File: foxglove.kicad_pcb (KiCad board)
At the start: 4 copper layers, 70.7 x 53.3 mm, 140 parts, among them IC1 LFE5U-12F-6BG256C, J1 NEIGHBOR1, J2 NEIGHBOR2, J3 Conn_02x05_Odd_Even, J4 Conn_02x05_Odd_Even, J5 Conn_01x02_Female, J6 Conn_02x03_Odd_Even, J7 BONUS_ROW, U1 LM393, U10 SHIFTER, U11 74HC4051, U12 SHIFTER, U13 74HC4051, U14 SHIFTER, U15 74HC4051, U16 SHIFTER, U17 74HC4051, U18 SHIFTER, U19 74HC4051, U2 ADP225, U20 SHIFTER, U21 74HC4051, U22 SHIFTER, U23 74HC4051, U24 SHIFTER, U25 74LVC1G53, U3 AP2127, U4 74LVC1G3157, U5 AP2127, U6 AP2127, U7 DAC084S085, U9 74HC4051

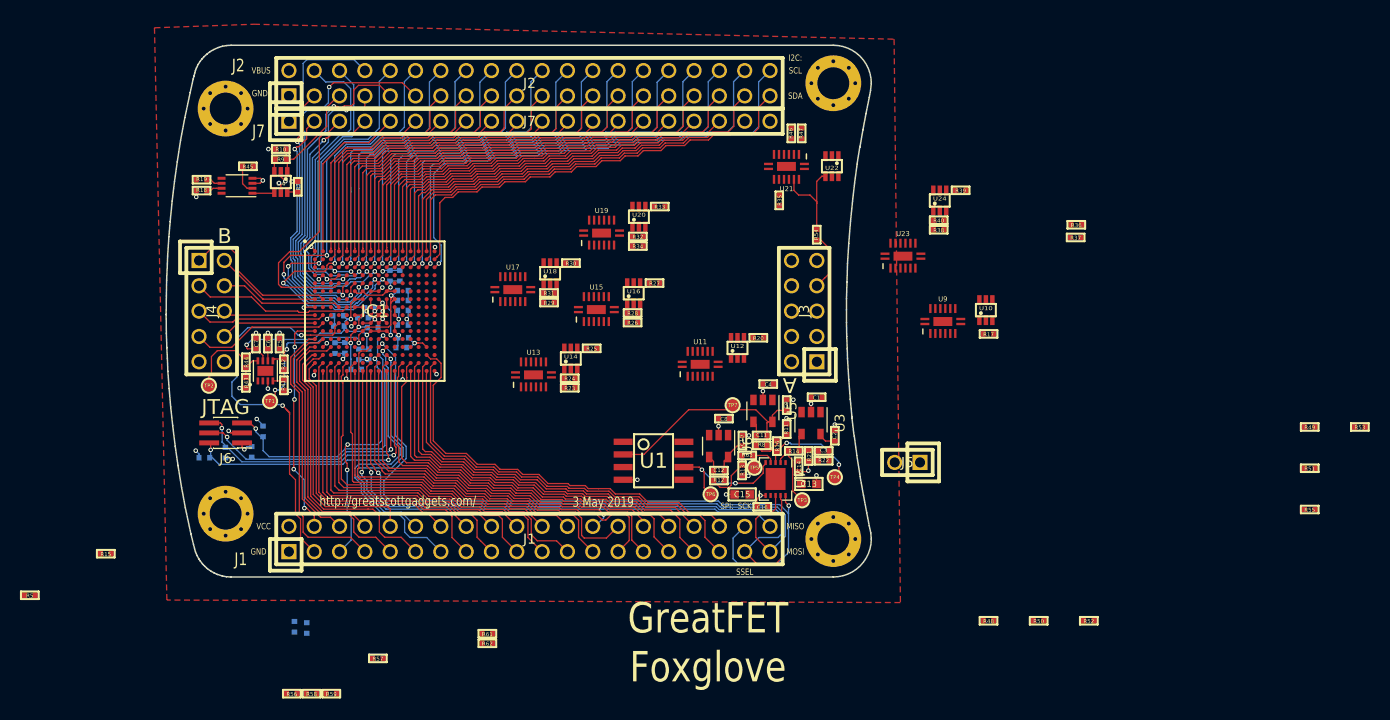
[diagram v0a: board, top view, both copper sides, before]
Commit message: Fixed sym-lib-table and continued routing bank A
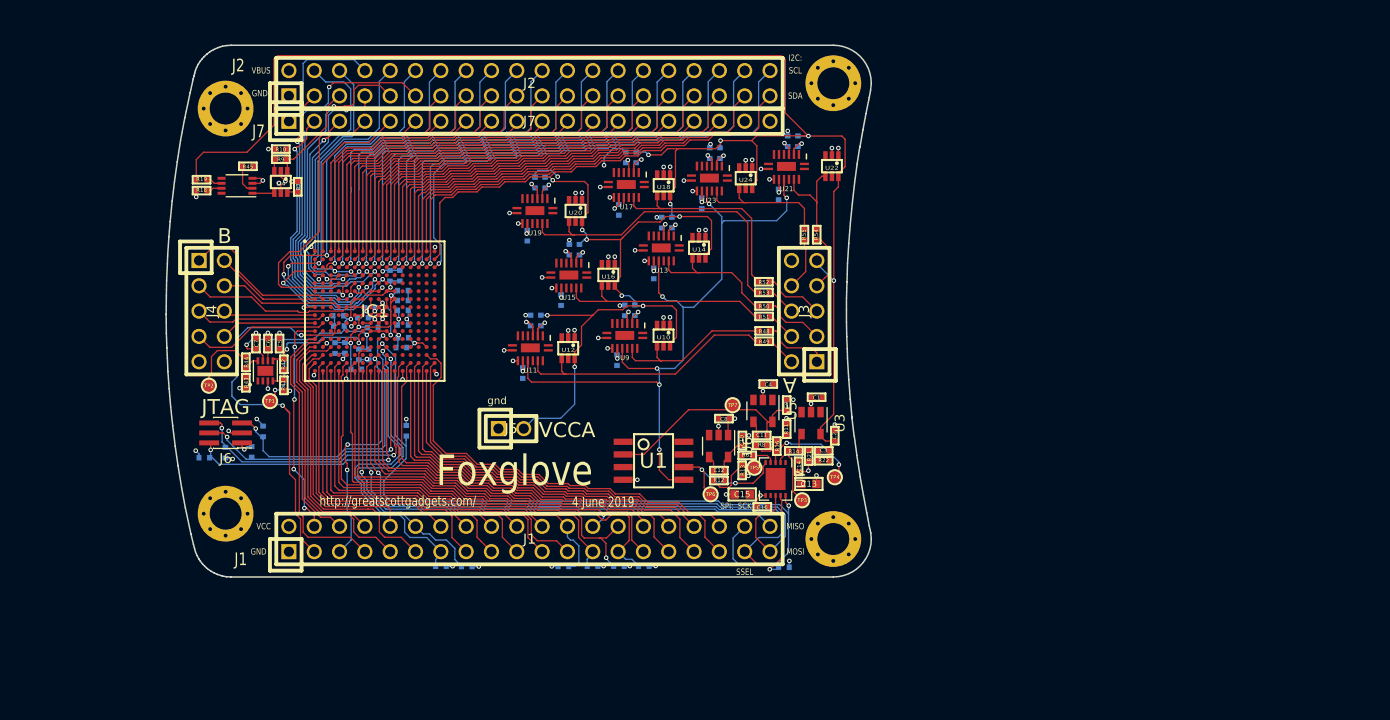
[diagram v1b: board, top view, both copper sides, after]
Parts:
- R15, R17, R20, R23, R24, R25, R26, R27, R28, R29, R30, R31, R32, R33, R34, R35, R36, R37, R38, R39, R40, R46, R47, R5, R56, R57, R58, R59, R61, R62: moved to B.Cu
- moved R15 68.0 mm to (171.6, 120.9), turned to 180 degrees
- moved R5 61.7 mm to (157.5, 120.8), turned to 180 degrees
- moved R53 61.3 mm to (169.6, 93.4)
- moved R55 57.7 mm to (173.6, 87.6), turned to 270 degrees
- moved R51 56.8 mm to (169.6, 95.8)
- moved R49 55.4 mm to (169.6, 98.3)
- moved R62 54.4 mm to (165.2, 79.4), turned to 270 degrees
- moved R61 53.1 mm to (164.1, 79.4), turned to 270 degrees
- moved R52 47.1 mm to (169.6, 92.3)
- moved R36 45.7 mm to (155.7, 79.8), turned to 270 degrees
- moved R37 44.8 mm to (156.8, 79.8), turned to 270 degrees
- moved R39 42.7 mm to (146.6, 82.4), turned to 270 degrees
- moved R50 41.9 mm to (169.6, 94.7)
- moved J5 39.9 mm to (144.2, 107.0), turned to 0 degrees
- moved R40 39.7 mm to (147.6, 82.4), turned to 270 degrees
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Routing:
- net /VCCA: track 4.07 -> 224.9 mm, vias 0 -> 13
- net /COMP2: track 0.00 -> 73.5 mm, vias 0 -> 6
- net Net-(R53-Pad1): track 0.00 -> 32.4 mm
- net GND: track 59.9 -> 87.1 mm, vias 46 -> 80
- net Net-(R49-Pad1): track 0.00 -> 27.0 mm
- net Net-(R51-Pad1): track 0.00 -> 21.9 mm
- net Net-(R52-Pad1): track 0.00 -> 21.7 mm
- net Net-(R48-Pad1): track 0.00 -> 16.8 mm
- net Net-(R55-Pad1): track 0.00 -> 14.0 mm
- net Net-(R50-Pad1): track 0.00 -> 14.0 mm
- net VCC: track 27.1 -> 39.0 mm, vias 10 -> 24
- net /CFG_1: track 25.1 -> 32.0 mm
- net /A1: track 0.00 -> 6.92 mm
- net /A3: track 0.00 -> 6.38 mm
- net /A5: track 0.00 -> 6.21 mm
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- removed copper zone on F.Cu, net +5V
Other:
- board text added: "4 June 2019"
- board text added: "Foxglove"
- board text added: "VCCA"
- board text added: "gnd"
- board text removed: "3 May 2019"
- board text removed: "GreatFET Foxglove"

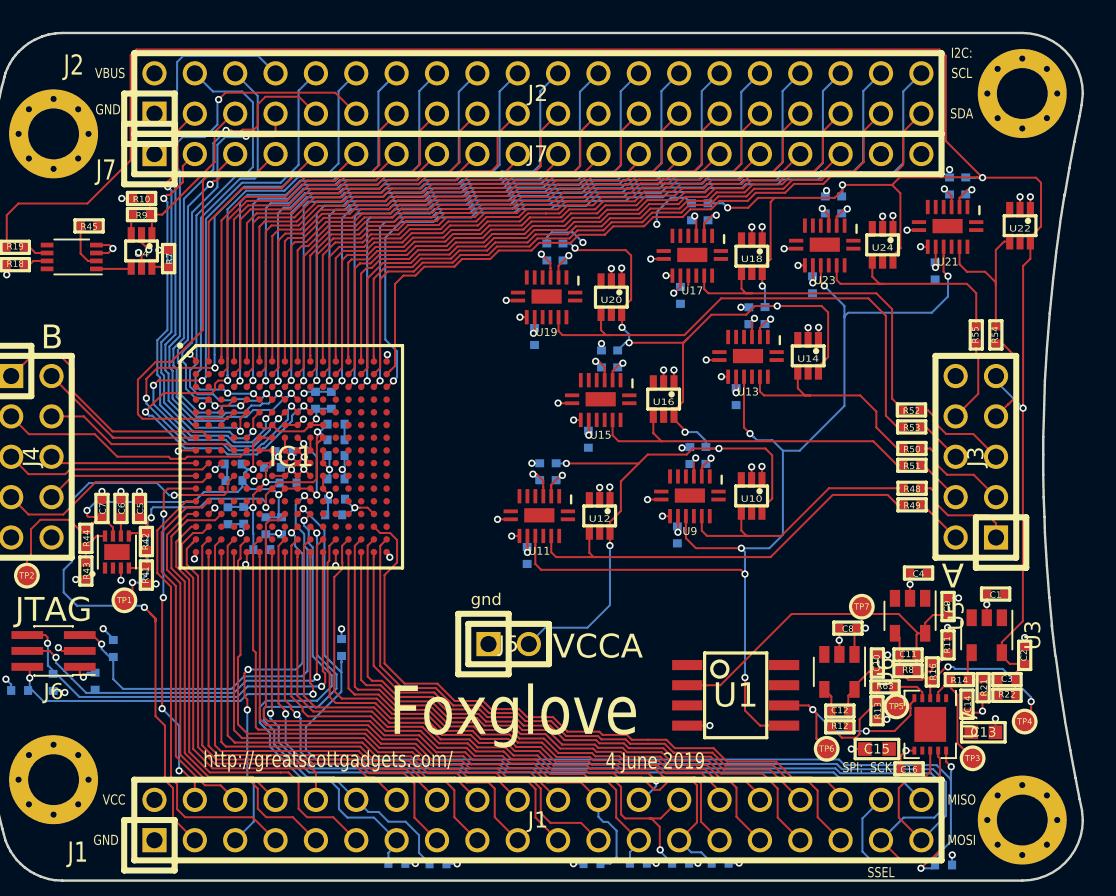
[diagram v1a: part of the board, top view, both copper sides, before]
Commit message: Changed headers for bank A and B, combined ADC voltage divider / pull-ups
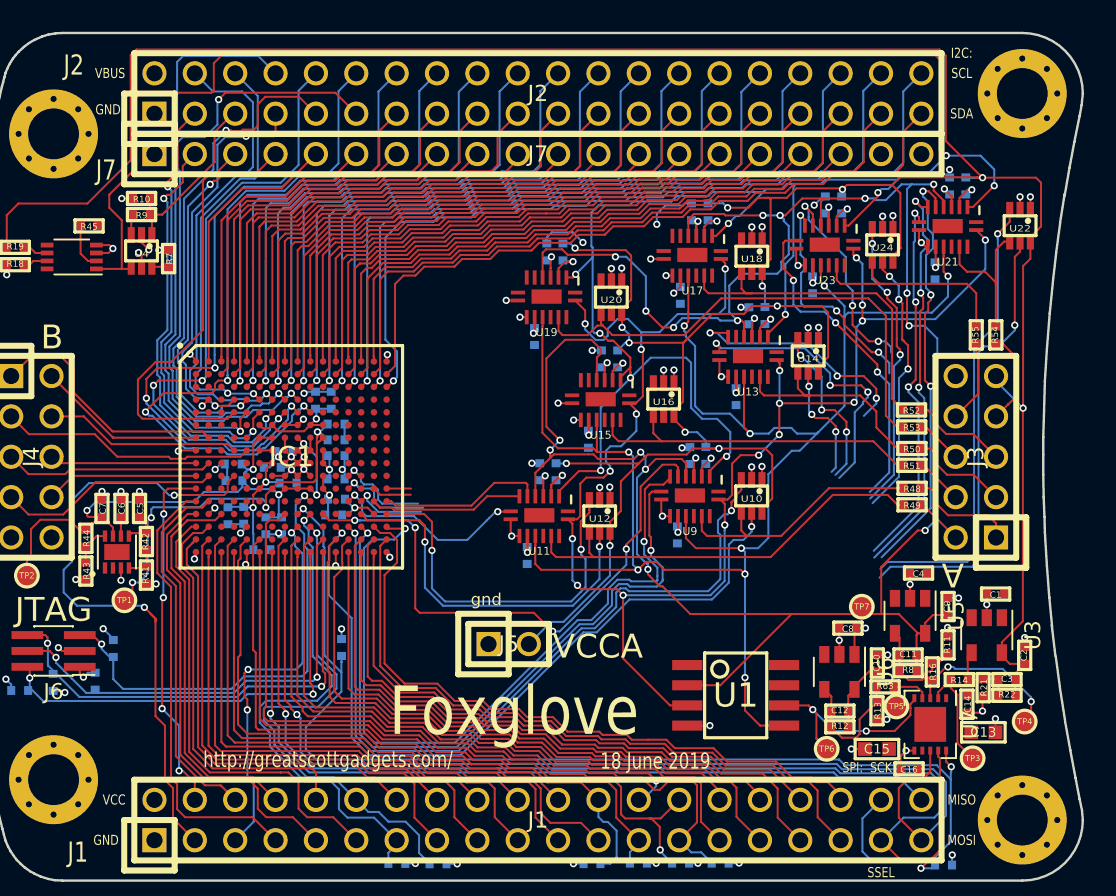
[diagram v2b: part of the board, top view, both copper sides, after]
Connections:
- IC1 pad K13: (no net) -> /S0_3
- IC1 pad L13: (no net) -> /S1_3
- IC1 pad L15: (no net) -> /DIR_3
- IC1 pad L16: (no net) -> /A3_shift
- IC1 pad M13: (no net) -> /S2_2
- IC1 pad M14: (no net) -> /S2_3
- IC1 pad M15: (no net) -> /S1_2
- IC1 pad M16: (no net) -> /S0_2
- IC1 pad N11: (no net) -> /S0_1
- IC1 pad N14: (no net) -> /DIR_2
- IC1 pad N16: (no net) -> /A2_shift
- IC1 pad P12: (no net) -> /DIR_1
- IC1 pad P13: (no net) -> /A1_shift
- IC1 pad P14: (no net) -> /S2_1
- IC1 pad P16: (no net) -> /S1_1
- U10 pad 3: (no net) -> /A1_shift
- U10 pad 5: (no net) -> /DIR_1
- U11 pad 10: (no net) -> /S1_2
- U11 pad 11: (no net) -> /S0_2
- U11 pad 9: (no net) -> /S2_2
- U12 pad 3: (no net) -> /A2_shift
- U12 pad 5: (no net) -> /DIR_2
- U13 pad 10: (no net) -> /S1_3
- U13 pad 11: (no net) -> /S0_3
- U13 pad 9: (no net) -> /S2_3
- U14 pad 3: (no net) -> /A3_shift
- U14 pad 5: (no net) -> /DIR_3
- U9 pad 10: (no net) -> /S1_1
- U9 pad 11: (no net) -> /S0_1
- U9 pad 9: (no net) -> /S2_1
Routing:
- net (no net): track 0.00 -> 217.4 mm, vias 0 -> 26
- net /ADC_A: track 2.25 -> 162.7 mm, vias 0 -> 10
- net /DAC: track 22.7 -> 148.1 mm, vias 0 -> 16
- net /COMP1: track 0.00 -> 99.1 mm, vias 0 -> 18
- net /A1_shift: track 0.00 -> 48.9 mm, vias 0 -> 2
- net /DIR_1: track 0.00 -> 48.5 mm, vias 0 -> 2
- net /S1_1: track 0.00 -> 47.6 mm, vias 0 -> 2
- net /S2_1: track 0.00 -> 44.4 mm, vias 0 -> 2
- net /COMP2: track 73.5 -> 110.9 mm, vias 6 -> 9
- net /S0_1: track 0.00 -> 35.7 mm, vias 0 -> 4
- net /A2_shift: track 0.00 -> 23.5 mm, vias 0 -> 2
- net /DIR_2: track 0.00 -> 23.3 mm, vias 0 -> 2
- net /S2_3: track 0.00 -> 22.6 mm, vias 0 -> 4
- net /S1_3: track 0.00 -> 21.3 mm, vias 0 -> 4
- net /S2_2: track 0.00 -> 12.6 mm, vias 0 -> 2
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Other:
- board text added: "18 June 2019"
- board text removed: "4 June 2019"

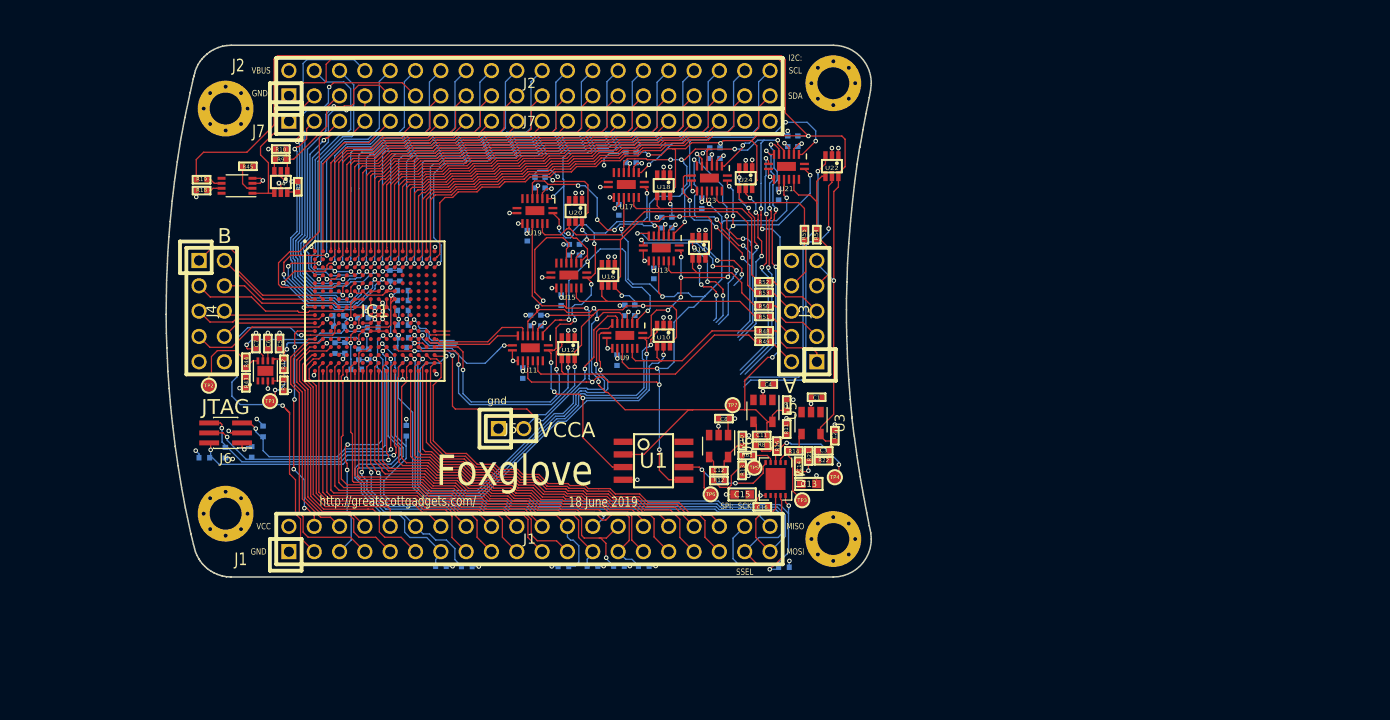
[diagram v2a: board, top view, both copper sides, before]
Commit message: Completed routing of new connectors.
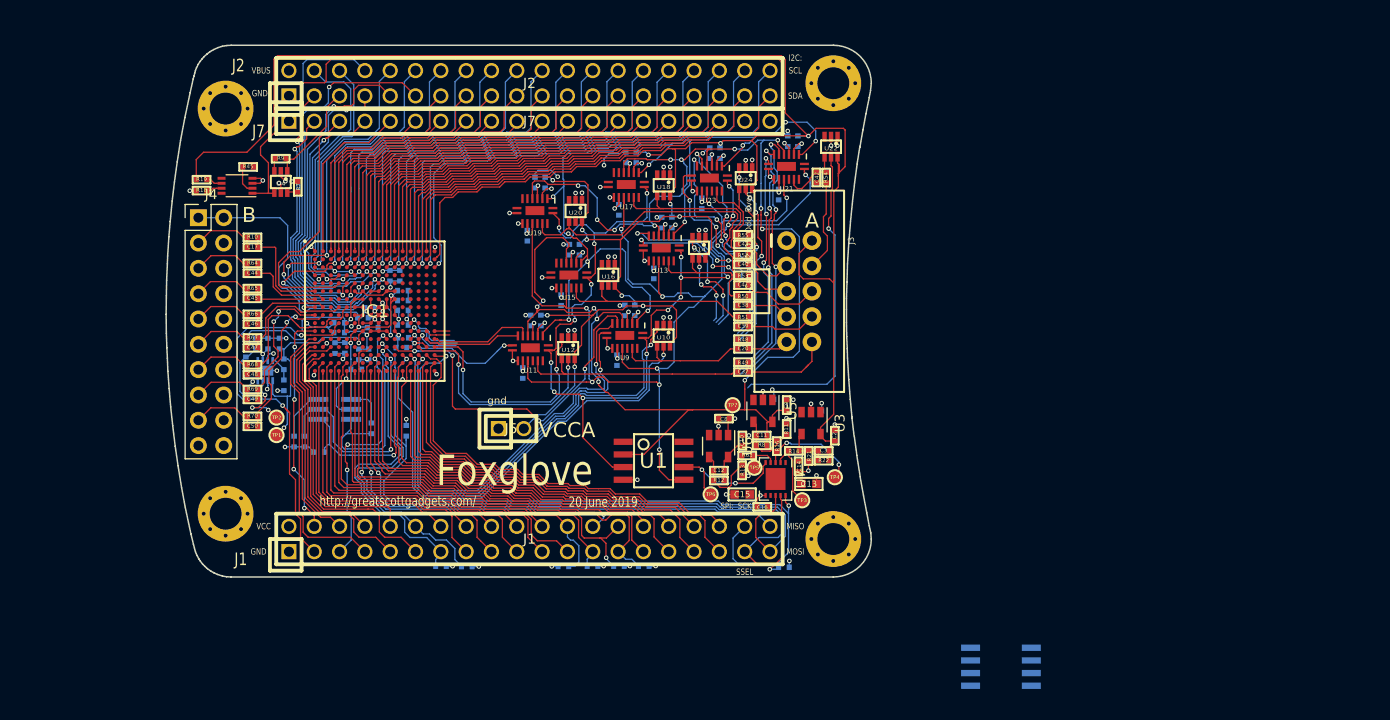
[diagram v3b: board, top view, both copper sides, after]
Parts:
- added C17: 0.1uF, gsg-modules:0402, F.Cu at (118.3, 88.8)
- added C20: 0.1uF, gsg-modules:0402, F.Cu at (167.5, 99.0)
- added C37: 0.1uF, gsg-modules:0402, F.Cu at (167.5, 101.4)
- added C38: 0.1uF, gsg-modules:0402, F.Cu at (167.5, 94.7)
- added C39: 0.1uF, gsg-modules:0402, F.Cu at (167.5, 96.8)
- added C40: 0.1uF, gsg-modules:0402, F.Cu at (167.5, 90.6)
- added C41: 0.1uF, gsg-modules:0402, F.Cu at (167.5, 92.6)
- added C42: 0.1uF, gsg-modules:0402, F.Cu at (174.8, 81.8)
- added C43: 0.1uF, gsg-modules:0402, F.Cu at (167.5, 88.6)
- added C44: 0.1uF, gsg-modules:0402, F.Cu at (118.3, 91.5)
- added C45: 0.1uF, gsg-modules:0402, F.Cu at (118.3, 94.0)
- added C46: 0.1uF, gsg-modules:0402, F.Cu at (118.3, 96.6)
- added C47: 0.1uF, gsg-modules:0402, F.Cu at (118.3, 98.9)
- added C48: 0.1uF, gsg-modules:0402, F.Cu at (118.3, 101.6)
- added C49: 0.1uF, gsg-modules:0402, F.Cu at (118.3, 104.1)
- added C50: 0.1uF, gsg-modules:0402, F.Cu at (118.3, 106.8)
- added R64: 100, gsg-modules:0402, F.Cu at (118.3, 90.5)
- added R65: 100, gsg-modules:0402, F.Cu at (118.3, 93.0)
- added R66: 100, gsg-modules:0402, F.Cu at (118.3, 95.6)
- added R67: 100, gsg-modules:0402, F.Cu at (118.3, 97.9)
- added R68: 100, gsg-modules:0402, F.Cu at (118.3, 100.6)
- added R69: 100, gsg-modules:0402, F.Cu at (118.3, 103.1)
- added R70: 100, gsg-modules:0402, F.Cu at (118.3, 105.8)
- added U8: AT25xxx, gsg-modules:SOIC8-154, B.Cu at (193.3, 130.9)
- C1, C4, C5, C6, C7, J6, R41, R42, R43, R44, U2: moved to B.Cu
- J3: footprint gsg-modules:HEADER-2x5 -> gsg-modules:2X5-SHROUDED
- J4: value Conn_02x05_Odd_Even -> Conn_02x10_Odd_Even; footprint gsg-modules:HEADER-2x5 -> Connector_PinHeader_2.54mm:PinHeader_2x10_P2.54mm_Vertical
- R10: value 10k -> 100
- R48, R49, R50, R51, R52, R53, R54, R55: value 0 -> 100
- moved J6 11.2 mm to (126.5, 105.1)
- moved R60 10.9 mm to (130.2, 107.0)
- moved J4 9.47 mm to (112.8, 85.9), turned to 0 degrees
- moved R1 9.41 mm to (125.0, 109.4), turned to 0 degrees
- moved R10 9.30 mm to (118.3, 87.8), turned to 180 degrees
- moved R2 9.15 mm to (122.4, 108.3), turned to 90 degrees
- moved TP2 7.50 mm to (120.7, 105.9)
- moved R55 6.16 mm to (167.5, 87.6), turned to 0 degrees
- moved R54 5.81 mm to (175.8, 81.9)
- moved R4 5.37 mm to (123.5, 108.3), turned to 90 degrees
- moved TP1 3.46 mm to (120.7, 107.7)
- moved R52 3.41 mm to (167.5, 89.6)
- moved R49 2.98 mm to (167.5, 100.4)
- moved R53 2.71 mm to (167.5, 91.7)
- moved R50 2.34 mm to (167.5, 93.7)
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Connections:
- net /ADC_sel renamed /div_sel
- IC1 pad B1: (no net) -> Net-(IC1-PadB1)
- IC1 pad B2: (no net) -> Net-(IC1-PadB2)
- IC1 pad C1: (no net) -> Net-(IC1-PadC1)
- IC1 pad C2: (no net) -> Net-(IC1-PadC2)
- IC1 pad C3: (no net) -> Net-(IC1-PadC3)
- IC1 pad D1: (no net) -> Net-(IC1-PadD1)
- IC1 pad D10: (no net) -> Net-(IC1-PadD10)
- IC1 pad D11: (no net) -> Net-(IC1-PadD11)
- IC1 pad D12: (no net) -> Net-(IC1-PadD12)
- IC1 pad D13: (no net) -> Net-(IC1-PadD13)
- IC1 pad D14: (no net) -> Net-(IC1-PadD14)
- IC1 pad D16: (no net) -> Net-(IC1-PadD16)
- IC1 pad D3: (no net) -> Net-(IC1-PadD3)
- IC1 pad E1: (no net) -> Net-(IC1-PadE1)
- IC1 pad E11: (no net) -> Net-(IC1-PadE11)
- IC1 pad E12: (no net) -> Net-(IC1-PadE12)
- IC1 pad E13: (no net) -> Net-(IC1-PadE13)
- IC1 pad E14: (no net) -> Net-(IC1-PadE14)
- IC1 pad E15: (no net) -> Net-(IC1-PadE15)
- IC1 pad E16: (no net) -> Net-(IC1-PadE16)
- IC1 pad E2: (no net) -> Net-(IC1-PadE2)
- IC1 pad E3: (no net) -> Net-(IC1-PadE3)
- IC1 pad F1: (no net) -> /B1_P
- IC1 pad F12: (no net) -> Net-(IC1-PadF12)
- IC1 pad F13: (no net) -> Net-(IC1-PadF13)
- IC1 pad F14: (no net) -> Net-(IC1-PadF14)
- IC1 pad F15: (no net) -> Net-(IC1-PadF15)
- IC1 pad F16: (no net) -> Net-(IC1-PadF16)
- IC1 pad F2: (no net) -> Net-(IC1-PadF2)
- IC1 pad F3: (no net) -> Net-(IC1-PadF3)
- IC1 pad F4: (no net) -> Net-(IC1-PadF4)
- IC1 pad F5: (no net) -> Net-(IC1-PadF5)
- IC1 pad G1: /B2 -> /B2_P
- IC1 pad G12: (no net) -> Net-(IC1-PadG12)
- IC1 pad G13: (no net) -> Net-(IC1-PadG13)
- IC1 pad G14: (no net) -> Net-(IC1-PadG14)
- IC1 pad G15: (no net) -> Net-(IC1-PadG15)
- IC1 pad G16: (no net) -> Net-(IC1-PadG16)
- IC1 pad G2: /B1 -> /B1_N
- IC1 pad G3: (no net) -> Net-(IC1-PadG3)
- IC1 pad G4: (no net) -> Net-(IC1-PadG4)
- IC1 pad G5: (no net) -> Net-(IC1-PadG5)
- IC1 pad H12: (no net) -> Net-(IC1-PadH12)
- IC1 pad H13: (no net) -> Net-(IC1-PadH13)
- IC1 pad H14: (no net) -> Net-(IC1-PadH14)
- IC1 pad H15: (no net) -> Net-(IC1-PadH15)
- IC1 pad H2: (no net) -> /B2_N
- IC1 pad H3: (no net) -> Net-(IC1-PadH3)
- IC1 pad H4: /B4 -> /B3_P
- IC1 pad H5: /B3 -> /B3_N
- IC1 pad J1: /B6 -> /B4_P
- IC1 pad J12: (no net) -> Net-(IC1-PadJ12)
- IC1 pad J13: (no net) -> Net-(IC1-PadJ13)
- IC1 pad J14: (no net) -> Net-(IC1-PadJ14)
- IC1 pad J15: (no net) -> Net-(IC1-PadJ15)
- IC1 pad J16: (no net) -> Net-(IC1-PadJ16)
- IC1 pad J2: /B5 -> /B4_N
- IC1 pad J3: (no net) -> Net-(IC1-PadJ3)
- IC1 pad J4: (no net) -> Net-(IC1-PadJ4)
- IC1 pad J5: (no net) -> Net-(IC1-PadJ5)
- IC1 pad K1: /B8 -> Net-(IC1-PadK1)
- IC1 pad K12: (no net) -> Net-(IC1-PadK12)
- IC1 pad K14: (no net) -> Net-(IC1-PadK14)
- IC1 pad K15: (no net) -> Net-(IC1-PadK15)
- IC1 pad K16: (no net) -> Net-(IC1-PadK16)
- IC1 pad K2: /B7 -> Net-(IC1-PadK2)
- IC1 pad K3: (no net) -> Net-(IC1-PadK3)
- IC1 pad K5: (no net) -> Net-(IC1-PadK5)
- IC1 pad L12: (no net) -> Net-(IC1-PadL12)
- IC1 pad L14: (no net) -> Net-(IC1-PadL14)
- IC1 pad L2: (no net) -> Net-(IC1-PadL2)
- IC1 pad L3: (no net) -> Net-(IC1-PadL3)
- IC1 pad L4: (no net) -> Net-(IC1-PadL4)
- IC1 pad L5: (no net) -> Net-(IC1-PadL5)
- IC1 pad M11: (no net) -> Net-(IC1-PadM11)
- IC1 pad M12: (no net) -> Net-(IC1-PadM12)
- IC1 pad M3: (no net) -> Net-(IC1-PadM3)
- IC1 pad M4: (no net) -> Net-(IC1-PadM4)
- IC1 pad M5: (no net) -> Net-(IC1-PadM5)
- IC1 pad M6: (no net) -> Net-(IC1-PadM6)
- IC1 pad M7: (no net) -> Net-(IC1-PadM7)
- IC1 pad M8: (no net) -> Net-(IC1-PadM8)
- IC1 pad M9: (no net) -> Net-(IC1-PadM9)
- IC1 pad N12: (no net) -> Net-(IC1-PadN12)
- IC1 pad N13: (no net) -> Net-(IC1-PadN13)
- IC1 pad N4: (no net) -> Net-(IC1-PadN4)
- IC1 pad N5: (no net) -> Net-(IC1-PadN5)
- IC1 pad N6: (no net) -> Net-(IC1-PadN6)
- IC1 pad N7: (no net) -> Net-(IC1-PadN7)
- IC1 pad P11: (no net) -> Net-(IC1-PadP11)
- IC1 pad P3: (no net) -> Net-(IC1-PadP3)
- IC1 pad P4: (no net) -> Net-(IC1-PadP4)
- IC1 pad P5: (no net) -> Net-(IC1-PadP5)
- IC1 pad P6: (no net) -> Net-(IC1-PadP6)
- IC1 pad P7: (no net) -> Net-(IC1-PadP7)
- IC1 pad P8: (no net) -> Net-(IC1-PadP8)
- IC1 pad R7: (no net) -> Net-(IC1-PadR7)
- J3 pad 1: /A1 -> GND
- J3 pad 10: GND -> /A2
- J3 pad 2: /A2 -> /VCCA
- J3 pad 3: /A3 -> /A8
- J3 pad 4: /A4 -> /A7
- J3 pad 7: /A7 -> /A3
- J3 pad 8: /A8 -> /A4
- J3 pad 9: /VCCA -> /A1
- J4 pad 1: /B1 -> /VCCB
- J4 pad 2: /B2 -> /VCCB
- J4 pad 3: /B3 -> /Sheet5D737161/target
- J4 pad 4: /B4 -> GND
- J4 pad 5: /B5 -> /sheet5D96E709/target
- J4 pad 6: /B6 -> GND
- J4 pad 7: /B7 -> /sheet5D9A1BD9/target
- J4 pad 8: /B8 -> GND
- J4 pad 9: /VCCB -> /sheet5D9A1BDA/target
- R10 pad 1: GND -> /B1_P
- R10 pad 2: /ADC -> /Sheet5D737161/target
- R45 pad 1: /EN_pull -> +5V
- R45 pad 2: +5V -> /pull_en
- R9 pad 1: Net-(R9-Pad1) -> /ADC
- R9 pad 2: /ADC -> Net-(R9-Pad2)
- U1 pad 1: (no net) -> /COUT1
- U1 pad 7: (no net) -> /COUT2
- U11 pad 2: (no net) -> Net-(U11-Pad2)
- U11 pad 4: (no net) -> Net-(U11-Pad4)
- U13 pad 2: (no net) -> Net-(U13-Pad2)
- U13 pad 4: (no net) -> Net-(U13-Pad4)
- U15 pad 10: (no net) -> /S1_4
- U15 pad 11: (no net) -> /S0_4
- U15 pad 2: (no net) -> Net-(U15-Pad2)
- U15 pad 4: (no net) -> Net-(U15-Pad4)
- U15 pad 9: (no net) -> /S2_4
- U16 pad 3: (no net) -> /A4_shift
- U16 pad 5: (no net) -> /DIR_4
- U17 pad 10: (no net) -> /S1_5
- U17 pad 11: (no net) -> /S0_5
- U17 pad 2: (no net) -> Net-(U17-Pad2)
- U17 pad 4: (no net) -> Net-(U17-Pad4)
- U17 pad 9: (no net) -> /S2_5
- U18 pad 3: (no net) -> /A5_shift
- U18 pad 5: (no net) -> /DIR_5
- U19 pad 10: (no net) -> /S1_6
- U19 pad 11: (no net) -> /S0_6
- U19 pad 2: (no net) -> Net-(U19-Pad2)
- U19 pad 4: (no net) -> Net-(U19-Pad4)
- U19 pad 9: (no net) -> /S2_6
- U20 pad 3: (no net) -> /A6_shift
- U20 pad 5: (no net) -> /DIR_6
- U21 pad 10: (no net) -> /S1_7
- U21 pad 11: (no net) -> /S0_7
- U21 pad 2: (no net) -> Net-(U21-Pad2)
- U21 pad 4: (no net) -> Net-(U21-Pad4)
- U21 pad 9: (no net) -> /S2_7
- U22 pad 3: (no net) -> /A7_shift
- U22 pad 5: (no net) -> /DIR_7
- U23 pad 10: (no net) -> /S1_8
- U23 pad 11: (no net) -> /S0_8
- U23 pad 2: (no net) -> Net-(U23-Pad2)
- U23 pad 4: (no net) -> Net-(U23-Pad4)
- U23 pad 9: (no net) -> /S2_8
- U24 pad 3: (no net) -> /A8_shift
- U24 pad 5: (no net) -> /DIR_8
- U25 pad 1: /ADC_A -> /ADC
- U25 pad 2: /EN_pull -> /pull_en
- U25 pad 5: (no net) -> /pull_sel
- U3 pad 3: (no net) -> /VCCA_EN
- U4 pad 3: Net-(R9-Pad1) -> Net-(R9-Pad2)
- U4 pad 5: VCC -> +5V
- U5 pad 3: (no net) -> /DAC2_EN
- U6 pad 3: (no net) -> /VCCB_EN
- U9 pad 2: (no net) -> Net-(U9-Pad2)
- U9 pad 4: (no net) -> Net-(U9-Pad4)
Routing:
- net (no net): track 217.4 -> 0.00 mm, vias 26 -> 0
- net /DIR_7: track 0.00 -> 31.7 mm, vias 0 -> 1
- net /S0_7: track 0.00 -> 26.7 mm, vias 0 -> 3
- net /VCCB: track 7.64 -> 33.5 mm
- net /S1_7: track 0.00 -> 25.5 mm, vias 0 -> 3
- net /TCK: track 28.7 -> 5.14 mm, vias 2 -> 0
- net /S2_7: track 0.00 -> 23.5 mm, vias 0 -> 3
- net /S2_8: track 0.00 -> 21.4 mm, vias 0 -> 3
- net /A8_shift: track 0.00 -> 18.5 mm, vias 0 -> 3
- net /DIR_8: track 0.00 -> 17.0 mm, vias 0 -> 3
- net /B3_N: track 0.00 -> 16.3 mm
- net /B3: track 16.2 -> 0.00 mm
- net /B4_N: track 0.00 -> 16.0 mm, vias 0 -> 2
- net /B1: track 15.9 -> 0.00 mm
- net /S1_8: track 0.00 -> 15.3 mm, vias 0 -> 3
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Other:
- board text added: "20 June 2019"
- board text removed: "18 June 2019"
